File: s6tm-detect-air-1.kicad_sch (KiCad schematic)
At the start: 67 parts, among them J1 Conn_01x04, J2 Conn_01x04, J4 TC2030, J5 Conn_01x04_Pin, J8 Conn_01x04, SW1 SW_Push, SW5 SW_Push, U1 HT753-1, U10 LMC6482, U2 SN65HVD230, U3 MiCS-5524, U4 LM73100, U5 004-1-0100, U6 STM32F103C8Tx, U7 ENS160, U8 SYS1002-H2, U9 HTU21, Y1 8M

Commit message: schem: add test points
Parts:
- added TP3, TP4, TP5, TP6, TP7: TestPoint, TestPoint:TestPoint_Pad_D2.0mm, symbol Connector:TestPoint
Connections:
- net RS_1: now also TP4.1
- net RS_2: now also TP5.1
- net S88_RX: now also TP7.1
- net at R6.1, U10.3 (+), U8.4 (RS2): now also TP6.1
- net at R2.1, U10.5 (+), U3.D (Rs1): now also TP3.1

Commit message: schem: run and fix erc
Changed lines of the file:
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@@
 	)
 	(junction
+		(at 209.55 129.54)
+		(diameter 0)
+		(color 0 0 0 0)
+	)
+	(junction
 		(at 74.93 71.12)
 		(diameter 0)
@@
 	)
 	(junction
+		(at 127 184.15)
+		(diameter 0)
+		(color 0 0 0 0)
+	)
+	(junction
 		(at 275.59 139.7)
 		(diameter 0)
@@
 	(wire
 		(pts
-			(xy 205.74 129.54) (xy 213.36 129.54)
+			(xy 205.74 129.54) (xy 209.55 129.54)
 		)
 		(stroke
@@
 	(wire
 		(pts
+			(xy 209.55 129.54) (xy 213.36 129.54)
+		)
+		(stroke
+			(width 0)
+			(type default)
+		)
+	)
+	(wire
+		(pts
 			(xy 259.08 45.72) (xy 260.35 45.72)
 		)
@@
 	)
 	(symbol
+		(lib_id "power:PWR_FLAG")
+		(at 209.55 129.54 0)
+		(unit 1)
+		(body_style 1)
+		(exclude_from_sim no)
+		(in_bom yes)
+		(on_board yes)
+		(in_pos_files yes)
+		(dnp no)
+		(fields_autoplaced yes)
+		(property "Reference" "#FLG06"
+			(at 209.55 127.635 0)
+			(hide yes)
+			(show_name no)
+			(do_not_autoplace no)
+			(effects
+				(font
+					(size 1.27 1.27)
+				)
+			)
+		)
+		(property "Value" "PWR_FLAG"
+			(at 209.5499 125.73 90)
+			(hide yes)
+			(show_name no)
+			(do_not_autoplace no)
+			(effects
+				(font
+					(size 1.27 1.27)
+				)
+				(justify left)
+			)
+		)
+		(property "Footprint" ""
+			(at 209.55 129.54 0)
+			(hide yes)
+			(show_name no)
+			(do_not_autoplace no)
+			(effects
+				(font
+					(size 1.27 1.27)
+				)
+			)
+		)
+		(property "Datasheet" ""
+			(at 209.55 129.54 0)
+			(hide yes)
+			(show_name no)
+			(do_not_autoplace no)
+			(effects
+				(font
+					(size 1.27 1.27)
+				)
+			)
+		)
+		(property "Description" "Special symbol for telling ERC where power comes from"
+			(at 209.55 129.54 0)
+			(hide yes)
+			(show_name no)
+			(do_not_autoplace no)
+			(effects
+				(font
+					(size 1.27 1.27)
+				)
+			)
+		)
+		(pin "1"
+		)
+		(instances
+			(project "s6tm-detect-air-1"
+				(path "/8d20b800-c106-4814-ab1a-7da2e31fcc85"
+					(reference "#FLG06")
+					(unit 1)
+				)
+			)
+		)
+	)
+	(symbol
 		(lib_id "power:GND")
 		(at 21.59 144.78 0)
@@
 					(unit 1)
 				)
+			)
+		)
+	)
+	(symbol
+		(lib_id "power:PWR_FLAG")
+		(at 127 184.15 90)
+		(unit 1)
+		(body_style 1)
+		(exclude_from_sim no)
+		(in_bom yes)
+		(on_board yes)
+		(in_pos_files yes)
+		(dnp no)
+		(fields_autoplaced yes)
+		(property "Reference" "#FLG05"
+			(at 125.095 184.15 0)
+			(hide yes)
+			(show_name no)
+			(do_not_autoplace no)
+			(effects
+				(font
+					(size 1.27 1.27)
+				)
+			)
+		)
+		(property "Value" "PWR_FLAG"
+			(at 123.19 184.1501 90)
+			(hide yes)
+			(show_name no)
+			(do_not_autoplace no)
+			(effects
+				(font
+					(size 1.27 1.27)
+				)
+				(justify left)
+			)
+		)
+		(property "Footprint" ""
+			(at 127 184.15 0)
+			(hide yes)
+			(show_name no)
+			(do_not_autoplace no)
+			(effects
+				(font
+					(size 1.27 1.27)
+				)
+			)
+		)
+		(property "Datasheet" ""
+			(at 127 184.15 0)
+			(hide yes)
+			(show_name no)
+			(do_not_autoplace no)
+			(effects
+				(font
+					(size 1.27 1.27)
+				)
+			)
+		)
+		(property "Description" "Special symbol for telling ERC where power comes from"
+			(at 127 184.15 0)
+			(hide yes)
+			(show_name no)
+			(do_not_autoplace no)
+			(effects
+				(font
+					(size 1.27 1.27)
+				)
+			)
+		)
+		(pin "1"
+		)
+		(instances
+			(project "s6tm-detect-air-1"
+				(path "/8d20b800-c106-4814-ab1a-7da2e31fcc85"
+					(reference "#FLG05")
+					(unit 1)
+				)

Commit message: schem: add missing footprints
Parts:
- J1, J2: footprint (none) -> Connector_PinHeader_2.54mm:PinHeader_1x04_P2.54mm_Horizontal
- R1, R2, R6: footprint (none) -> Resistor_SMD:R_0402_1005Metric
- U10: footprint (none) -> Package_SO:SOIC-8_3.9x4.9mm_P1.27mm
- U8: footprint Crystal_SMD_3225-4Pin_3.2x2.5mm -> Crystal:Crystal_SMD_3225-4Pin_3.2x2.5mm
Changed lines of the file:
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@@
 			)
 		)
-		(property "Footprint" ""
+		(property "Footprint" "Connector_PinHeader_2.54mm:PinHeader_1x04_P2.54mm_Horizontal"
 			(at 77.47 151.13 0)
 			(hide yes)
@@
 			)
 		)
-		(property "Footprint" ""
+		(property "Footprint" "Resistor_SMD:R_0402_1005Metric"
 			(at 23.368 73.66 90)
 			(hide yes)
@@
 			)
 		)
-		(property "Footprint" ""
+		(property "Footprint" "Package_SO:SOIC-8_3.9x4.9mm_P1.27mm"
 			(at 66.04 71.12 0)
 			(hide yes)
@@
 			)
 		)
-		(property "Footprint" ""
+		(property "Footprint" "Resistor_SMD:R_0402_1005Metric"
 			(at 51.562 104.14 90)
 			(hide yes)
@@
 			)
 		)
-		(property "Footprint" ""
+		(property "Footprint" "Resistor_SMD:R_0402_1005Metric"
 			(at 45.212 73.66 90)
 			(hide yes)
@@
 			)
 		)
-		(property "Footprint" ""
+		(property "Footprint" "Connector_PinHeader_2.54mm:PinHeader_1x04_P2.54mm_Horizontal"
 			(at 22.86 40.64 0)
 			(hide yes)
@@
 			)
 		)
-		(property "Footprint" "Crystal_SMD_3225-4Pin_3.2x2.5mm"
+		(property "Footprint" "Crystal:Crystal_SMD_3225-4Pin_3.2x2.5mm"
 			(at 34.29 68.58 0)
 			(hide yes)
@@
 			)
 		)
-		(property "Footprint" ""
+		(property "Footprint" "Package_SO:SOIC-8_3.9x4.9mm_P1.27mm"
 			(at 73.66 101.6 0)
 			(hide yes)
@@
 			)
 		)
-		(property "Footprint" ""
+		(property "Footprint" "Package_SO:SOIC-8_3.9x4.9mm_P1.27mm"
 			(at 102.87 127 0)
 			(hide yes)

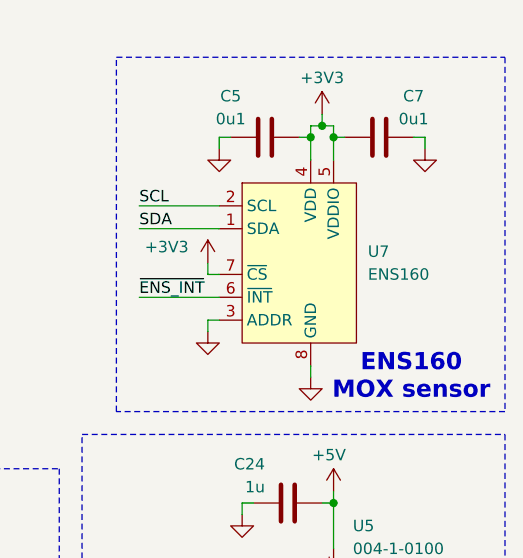
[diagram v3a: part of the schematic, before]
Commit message: schem: add ENS160 footprint
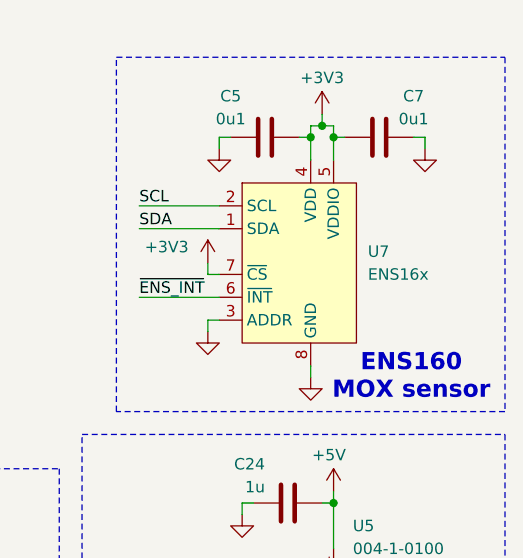
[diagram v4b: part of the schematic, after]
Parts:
- U7: value ENS160 -> ENS16x; footprint (none) -> GLCS:Sciosense_ENS160_LGA_9_3x3mm
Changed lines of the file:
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@@
 			)
 		)
-		(property "Value" "ENS160"
+		(property "Value" "ENS16x"
 			(at 266.7 60.9599 0)
 			(show_name no)
@@
 			)
 		)
-		(property "Footprint" ""
+		(property "Footprint" "GLCS:Sciosense_ENS160_LGA_9_3x3mm"
 			(at 262.89 66.04 0)
 			(hide yes)

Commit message: schem: fix potentiometer footprints
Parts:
- R2, R6: footprint Resistor_SMD:R_0402_1005Metric -> Potentiometer_THT:Potentiometer_Bourns_3296W_Vertical
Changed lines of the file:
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@@
 			)
 		)
-		(property "Footprint" "Resistor_SMD:R_0402_1005Metric"
+		(property "Footprint" "Potentiometer_THT:Potentiometer_Bourns_3296W_Vertical"
 			(at 51.562 104.14 90)
 			(hide yes)
@@
 			)
 		)
-		(property "Footprint" "Resistor_SMD:R_0402_1005Metric"
+		(property "Footprint" "Potentiometer_THT:Potentiometer_Bourns_3296W_Vertical"
 			(at 45.212 73.66 90)
 			(hide yes)

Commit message: schem: add ordering info to BOM
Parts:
- J1, J2, R2, R6, U5: now left out of the parts list
- R1: Basic (none) -> Y; JLCPCB Part # (none) -> C25076; Manufacturer (none) -> Uniroyal Elec; Manufacturer Part Number (none) -> 0402WGF1000TCE
- U10: Basic (none) -> X; JLCPCB Part # (none) -> C95583; Manufacturer (none) -> Texas Instruments; Manufacturer Part Number (none) -> LMC6482IMX/NOPB
- U3: Basic (none) -> X; JLCPCB Part # (none) -> C3659348; Manufacturer (none) -> Amphenol ICC; Manufacturer Part Number (none) -> MICS-5524
- U7: Basic (none) -> X; JLCPCB Part # (none) -> C3659288; Manufacturer (none) -> Sciosense; Manufacturer Part Number (none) -> ENS160-BGLM
- U8: Basic (none) -> Xé; JLCPCB Part # (none) -> C5184223; Manufacturer (none) -> Saiya Sensor; Manufacturer Part Number (none) -> SYS1002-H2

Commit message: schem: add title
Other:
- company: (none) -> Rémi Ait-Younes
- title: (none) -> S6TM Detect air 1
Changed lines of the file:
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@@
 	(generator_version "10.0")
 	(paper "A4")
+	(title_block
+		(title "S6TM Detect air 1")
+		(date "2026-04-11")
+		(rev "01")
+		(company "Rémi Ait-Younes")
+	)
 	(rectangle
 		(start 54.61 58.42)

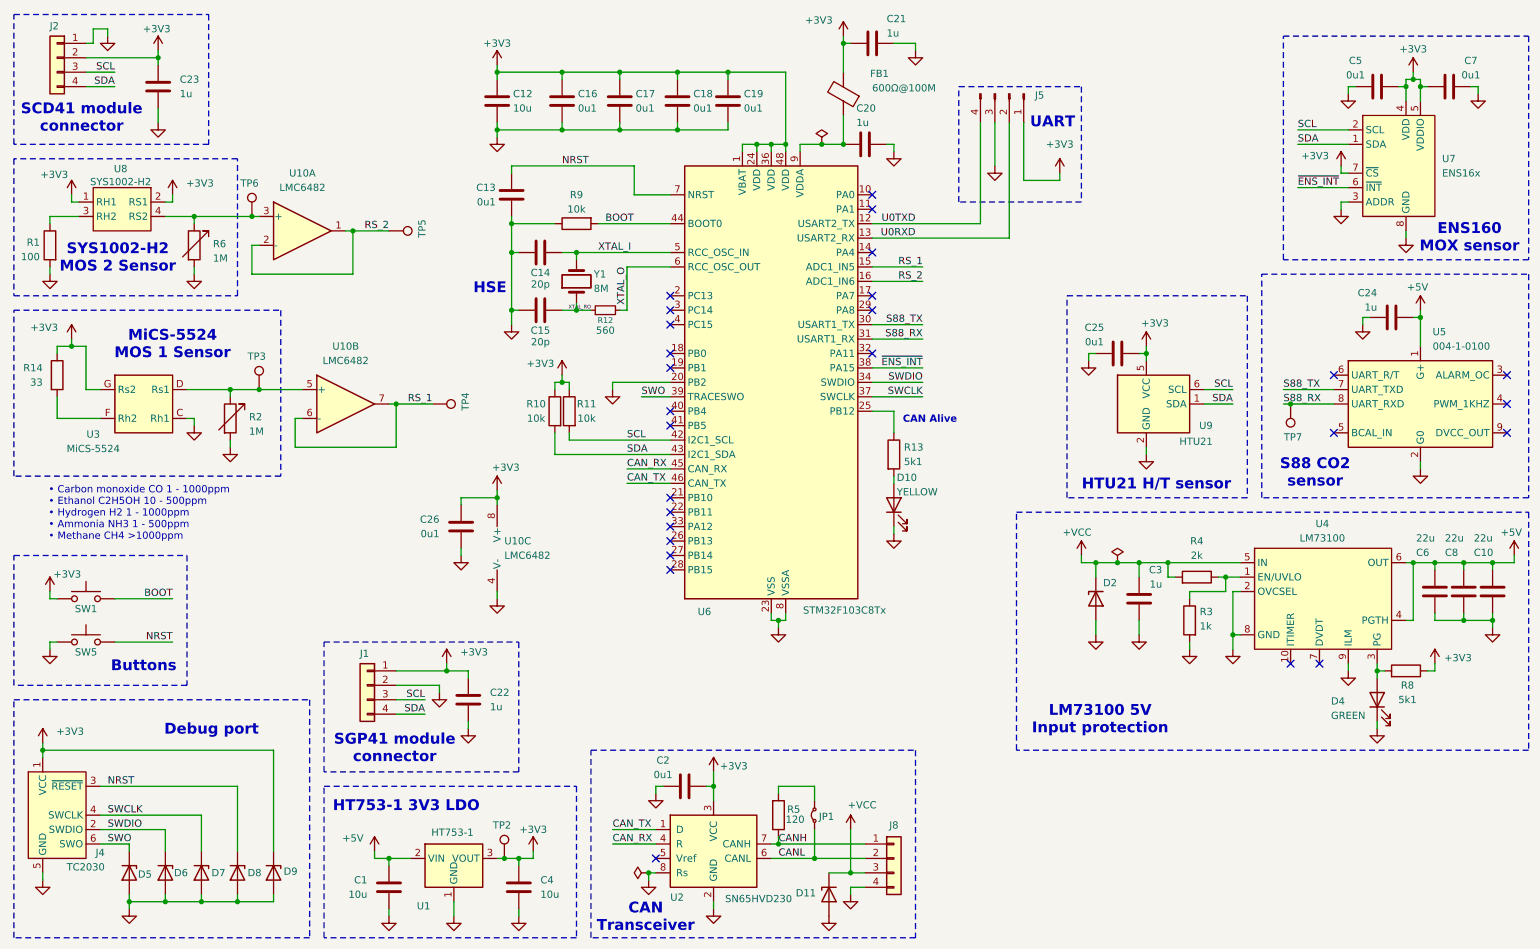
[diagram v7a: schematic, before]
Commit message: schem: renumber
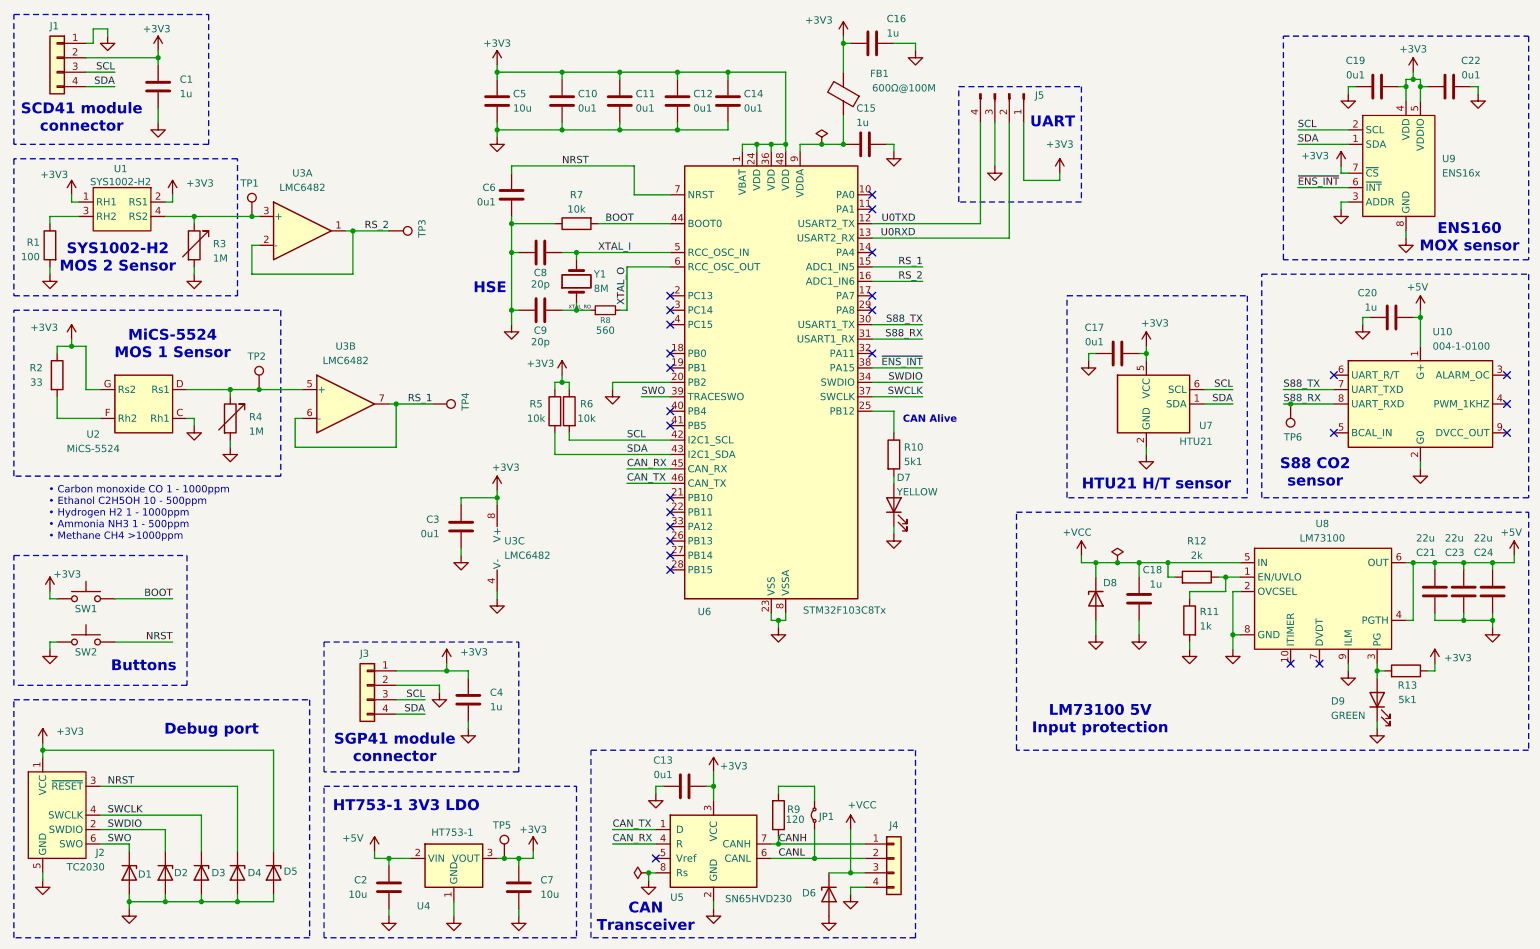
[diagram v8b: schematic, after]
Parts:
- renumbered C23 to C1, C16 to C10, C17 to C11, C18 to C12, C2 to C13, C19 to C14, C20 to C15, C21 to C16, C25 to C17, C3 to C18, C5 to C19, C1 to C2, C24 to C20, C6 to C21, C7 to C22, C8 to C23, C10 to C24, C26 to C3, C22 to C4, C12 to C5, C13 to C6, C4 to C7, C14 to C8, C15 to C9, D5 to D1, D6 to D2, D7 to D3, D8 to D4, D9 to D5, D11 to D6, D10 to D7, D2 to D8, D4 to D9, J2 to J1, J4 to J2, J1 to J3, J8 to J4, R13 to R10, R3 to R11, R4 to R12, R8 to R13, R14 to R2, R6 to R3, R2 to R4, R10 to R5, R11 to R6, R9 to R7, R12 to R8, R5 to R9, SW5 to SW2, TP6 to TP1, TP3 to TP2, TP5 to TP3, TP2 to TP5, TP7 to TP6, U8 to U1, U5 to U10, U3 to U2, U10 to U3, U1 to U4, U2 to U5, U9 to U7, U4 to U8, U7 to U9
